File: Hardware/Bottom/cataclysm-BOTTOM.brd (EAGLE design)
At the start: 33 x 33 mm, 37 parts, among them U4 PCF8523

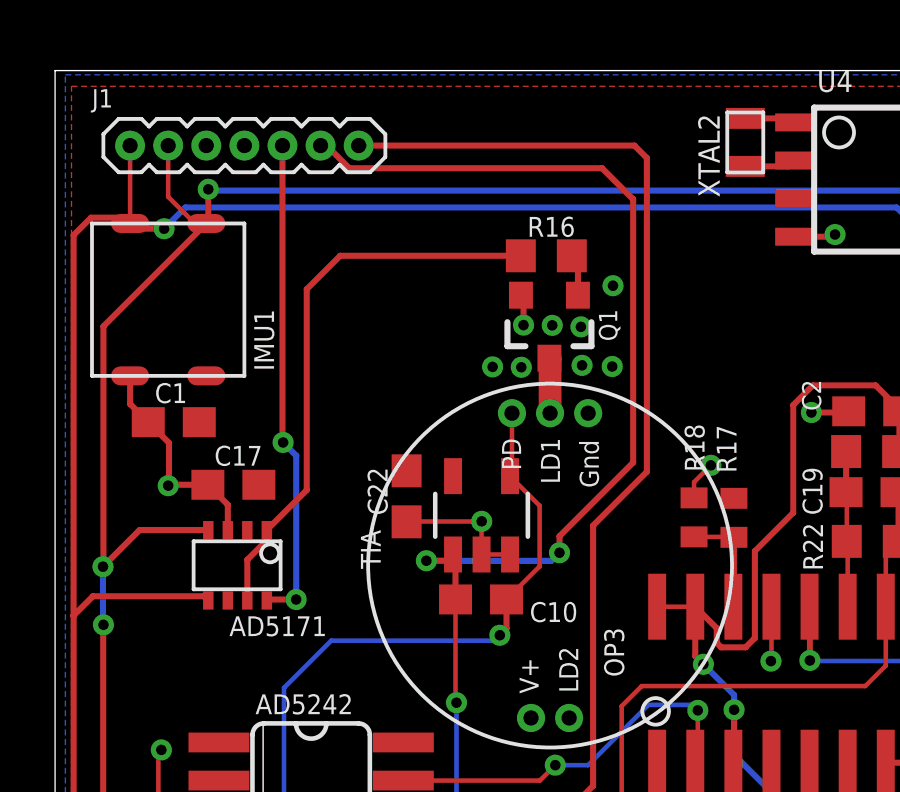
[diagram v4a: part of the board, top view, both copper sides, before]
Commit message: Fixed connection b/w top and bottom boards
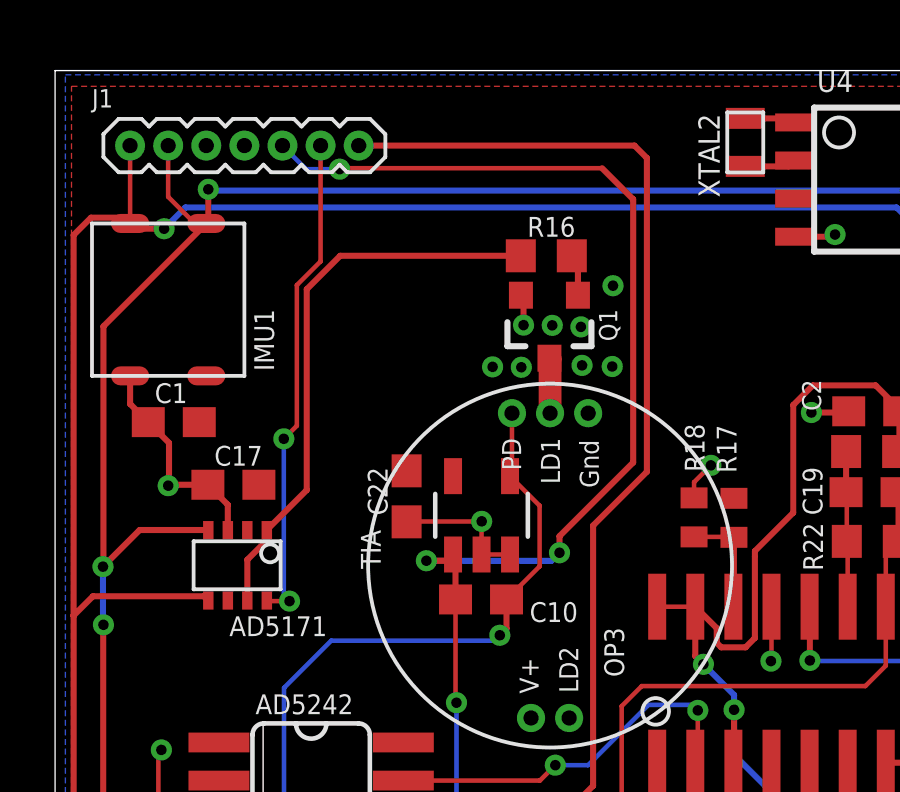
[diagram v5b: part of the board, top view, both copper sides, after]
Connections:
- removed net A5/TIA: AD5242.3, C10.2, C15.1, J1.6, TIA.1
- removed net D30/LED.CTRL: AD5171.8, J1.5
- new net A6/TIA: AD5242.3, C10.2, C15.1, J1.5, TIA.1
- new net D29/LED.CTRL: AD5171.8, J1.6
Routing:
- net A6/TIA: track 0.00 -> 64.5 mm, vias 0 -> 5
- net A5/TIA: track 63.2 -> 0.00 mm, vias 4 -> 0
- net D29/LED.CTRL: track 0.00 -> 16.5 mm, vias 0 -> 2
- net D30/LED.CTRL: track 16.3 -> 0.00 mm, vias 2 -> 0
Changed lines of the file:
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@@
 <wire x1="7.6073" y1="30.469834375" x2="7.504434375" y2="30.36696875" width="0.2" layer="1"/>
-</signal>
-<signal name="A5/TIA">
-<contactref element="C10" pad="2"/>
-<contactref element="AD5242" pad="3"/>
-<contactref element="C15" pad="1"/>
-<contactref element="TIA" pad="1"/>
-<wire x1="15.765746875" y1="19.36960625" x2="15.847965625" y2="19.2873875" width="0.1524" layer="1"/>
-<wire x1="15.847965625" y1="19.2873875" x2="15.847965625" y2="19.15668125" width="0.1524" layer="1"/>
-<wire x1="15.847965625" y1="17.871440625" x2="15.847965625" y2="17.7927" width="0.1524" layer="1"/>
-<wire x1="15.847965625" y1="17.7927" x2="15.847965625" y2="14.46185625" width="0.1524" layer="1"/>
-<wire x1="15.847965625" y1="14.46185625" x2="15.88008125" y2="14.429740625" width="0.1524" layer="1"/>
-<via x="15.88008125" y="14.429740625" extent="1-16" drill="0.35"/>
-<wire x1="15.88008125" y1="14.429740625" x2="15.88008125" y2="9.6926375" width="0.1524" layer="16"/>
-<wire x1="15.88008125" y1="9.6926375" x2="15.9004" y2="9.67231875" width="0.1524" layer="16"/>
-<via x="15.9004" y="9.67231875" extent="1-16" drill="0.35"/>
-<wire x1="15.9004" y1="9.67231875" x2="21.435053125" y2="4.137665625" width="0.1524" layer="1"/>
-<wire x1="29.11184375" y1="4.137665625" x2="21.435053125" y2="4.137665625" width="0.1524" layer="1"/>
-<wire x1="29.11184375" y1="4.137665625" x2="29.13978125" y2="4.165603125" width="0.1524" layer="1"/>
-<wire x1="8.577584375" y1="9.949178125" x2="7.962903125" y2="10.563859375" width="0.1524" layer="1"/>
-<wire x1="15.9004" y1="9.67231875" x2="15.623540625" y2="9.949178125" width="0.1524" layer="1"/>
-<wire x1="15.623540625" y1="9.949178125" x2="8.577584375" y2="9.949178125" width="0.1524" layer="1"/>
-<contactref element="J1" pad="6"/>
-<wire x1="11.35" y1="33" x2="11.55368125" y2="33" width="0.2032" layer="1"/>
-<wire x1="11.55368125" y1="33" x2="12.30768125" y2="32.246" width="0.2032" layer="1"/>
-<wire x1="20.73331875" y1="32.246" x2="21.77034375" y2="31.208975" width="0.2032" layer="1"/>
-<wire x1="12.30768125" y1="32.246" x2="20.73331875" y2="32.246" width="0.2032" layer="1"/>
-<wire x1="21.77034375" y1="31.208975" x2="21.77034375" y2="22.435821875" width="0.2032" layer="1"/>
-<wire x1="21.77034375" y1="22.435821875" x2="19.314159375" y2="19.9796375" width="0.2032" layer="1"/>
-<wire x1="19.314159375" y1="19.9796375" x2="19.314159375" y2="19.428459375" width="0.2032" layer="1"/>
-<via x="19.314159375" y="19.428459375" extent="1-16" drill="0.35"/>
-<wire x1="19.314159375" y1="19.428459375" x2="19.04238125" y2="19.15668125" width="0.2032" layer="16"/>
-<wire x1="15.847965625" y1="19.15668125" x2="15.847965625" y2="17.7927" width="0.2032" layer="1"/>
-<wire x1="19.04238125" y1="19.15668125" x2="14.881859375" y2="19.15668125" width="0.2032" layer="16"/>
-<wire x1="14.881859375" y1="19.15668125" x2="14.87678125" y2="19.161759375" width="0.2032" layer="16"/>
-<via x="14.87678125" y="19.161759375" extent="1-16" drill="0.35"/>
-<wire x1="14.87678125" y1="19.161759375" x2="15.8428875" y2="19.161759375" width="0.2032" layer="1"/>
-<wire x1="15.8428875" y1="19.161759375" x2="15.847965625" y2="19.15668125" width="0.2032" layer="1"/>
 </signal>
 <signal name="PD.C">
@@
 <wire x1="9.558021875" y1="19.845021875" x2="8.908021875" y2="19.195021875" width="0.2032" layer="1"/>
 </signal>
-<signal name="D30/LED.CTRL">
-<contactref element="AD5171" pad="8"/>
+<signal name="A6/TIA">
 <contactref element="J1" pad="5"/>
-<wire x1="10.08" y1="33" x2="10.08" y2="23.125421875" width="0.2032" layer="1"/>
-<wire x1="10.08" y1="23.125421875" x2="10.10158125" y2="23.103840625" width="0.2032" layer="1"/>
-<via x="10.10158125" y="23.103840625" extent="1-16" drill="0.35"/>
-<wire x1="10.10158125" y1="23.103840625" x2="10.541003125" y2="22.66441875" width="0.2032" layer="16"/>
-<wire x1="10.541003125" y1="22.66441875" x2="10.541003125" y2="17.873984375" width="0.2032" layer="16"/>
-<wire x1="10.541003125" y1="17.873984375" x2="10.53591875" y2="17.8689" width="0.2032" layer="16"/>
-<via x="10.53591875" y="17.8689" extent="1-16" drill="0.35"/>
-<wire x1="10.53591875" y1="17.8689" x2="9.593959375" y2="17.8689" width="0.2032" layer="1"/>
-<wire x1="9.593959375" y1="17.8689" x2="9.558021875" y2="17.8329625" width="0.2032" layer="1"/>
+<contactref element="AD5242" pad="3"/>
+<contactref element="C10" pad="2"/>
+<contactref element="C15" pad="1"/>
+<contactref element="TIA" pad="1"/>
+<wire x1="15.765746875" y1="19.36960625" x2="15.847965625" y2="19.2873875" width="0.1524" layer="1"/>
+<wire x1="15.847965625" y1="19.2873875" x2="15.847965625" y2="19.15668125" width="0.1524" layer="1"/>
+<wire x1="15.847965625" y1="17.871440625" x2="15.847965625" y2="17.7927" width="0.1524" layer="1"/>
+<wire x1="15.847965625" y1="17.7927" x2="15.847965625" y2="14.46185625" width="0.1524" layer="1"/>
+<wire x1="15.847965625" y1="14.46185625" x2="15.88008125" y2="14.429740625" width="0.1524" layer="1"/>
+<via x="15.88008125" y="14.429740625" extent="1-16" drill="0.35"/>
+<wire x1="15.88008125" y1="14.429740625" x2="15.88008125" y2="9.6926375" width="0.1524" layer="16"/>
+<wire x1="15.88008125" y1="9.6926375" x2="15.9004" y2="9.67231875" width="0.1524" layer="16"/>
+<via x="15.9004" y="9.67231875" extent="1-16" drill="0.35"/>
+<wire x1="15.9004" y1="9.67231875" x2="21.435053125" y2="4.137665625" width="0.1524" layer="1"/>
+<wire x1="29.11184375" y1="4.137665625" x2="21.435053125" y2="4.137665625" width="0.1524" layer="1"/>
+<wire x1="29.11184375" y1="4.137665625" x2="29.13978125" y2="4.165603125" width="0.1524" layer="1"/>
+<wire x1="15.9004" y1="9.67231875" x2="15.623540625" y2="9.949178125" width="0.1524" layer="1"/>
+<wire x1="15.623540625" y1="9.949178125" x2="8.577584375" y2="9.949178125" width="0.1524" layer="1"/>
+<wire x1="21.77034375" y1="31.208975" x2="20.73331875" y2="32.246" width="0.2032" layer="1"/>
+<wire x1="21.77034375" y1="31.208975" x2="21.77034375" y2="22.435821875" width="0.2032" layer="1"/>
+<wire x1="21.77034375" y1="22.435821875" x2="19.314159375" y2="19.9796375" width="0.2032" layer="1"/>
+<wire x1="19.314159375" y1="19.9796375" x2="19.314159375" y2="19.428459375" width="0.2032" layer="1"/>
+<via x="19.314159375" y="19.428459375" extent="1-16" drill="0.35"/>
+<wire x1="19.314159375" y1="19.428459375" x2="19.04238125" y2="19.15668125" width="0.2032" layer="16"/>
+<wire x1="15.847965625" y1="19.15668125" x2="15.847965625" y2="17.7927" width="0.2032" layer="1"/>
+<wire x1="19.04238125" y1="19.15668125" x2="14.881859375" y2="19.15668125" width="0.2032" layer="16"/>
+<wire x1="14.881859375" y1="19.15668125" x2="14.87678125" y2="19.161759375" width="0.2032" layer="16"/>
+<via x="14.87678125" y="19.161759375" extent="1-16" drill="0.35"/>
+<wire x1="14.87678125" y1="19.161759375" x2="15.8428875" y2="19.161759375" width="0.2032" layer="1"/>
+<wire x1="15.8428875" y1="19.161759375" x2="15.847965625" y2="19.15668125" width="0.2032" layer="1"/>
+<wire x1="20.73331875" y1="32.246" x2="12.01756875" y2="32.246" width="0.1524" layer="1"/>
+<wire x1="12.01756875" y1="32.246" x2="11.985" y2="32.21343125" width="0.1524" layer="1"/>
+<via x="11.985" y="32.21343125" extent="1-16" drill="0.35"/>
+<wire x1="11.985" y1="32.21343125" x2="10.86656875" y2="32.21343125" width="0.1524" layer="16"/>
+<wire x1="10.86656875" y1="32.21343125" x2="10.08" y2="33" width="0.1524" layer="16"/>
+<wire x1="8.577584375" y1="9.949178125" x2="7.962903125" y2="10.563859375" width="0.1524" layer="1"/>
 </signal>
 <signal name="N$10">
@@
 <wire x1="27.017296875" y1="33.9063625" x2="27.15181875" y2="33.771840625" width="0.2" layer="1"/>
 </signal>
+<signal name="D29/LED.CTRL">
+<contactref element="J1" pad="6"/>
+<contactref element="AD5171" pad="8"/>
+<via x="10.124440625" y="23.225759375" extent="1-16" drill="0.35"/>
+<wire x1="11.35" y1="33" x2="11.35" y2="29.139775" width="0.1524" layer="1"/>
+<wire x1="11.35" y1="29.139775" x2="10.55878125" y2="28.34855625" width="0.1524" layer="1"/>
+<wire x1="10.55878125" y1="23.6601" x2="10.124440625" y2="23.225759375" width="0.1524" layer="1"/>
+<wire x1="10.55878125" y1="28.34855625" x2="10.55878125" y2="23.6601" width="0.1524" layer="1"/>
+<wire x1="10.124440625" y1="23.225759375" x2="10.124440625" y2="18.006059375" width="0.1524" layer="16"/>
+<wire x1="10.124440625" y1="18.006059375" x2="10.314940625" y2="17.815559375" width="0.1524" layer="16"/>
+<via x="10.314940625" y="17.815559375" extent="1-16" drill="0.35"/>
+<wire x1="10.314940625" y1="17.815559375" x2="9.575425" y2="17.815559375" width="0.1524" layer="1"/>
+<wire x1="9.575425" y1="17.815559375" x2="9.558021875" y2="17.8329625" width="0.1524" layer="1"/>
+</signal>
 </signals>
